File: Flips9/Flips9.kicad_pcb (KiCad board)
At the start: 2 copper layers, 100 x 100 mm, 45 parts, among them CN1 UFP2810, U1 74238, U11 74238, U12 74238, U13 TD62783, U14 ULN2803/2003, U21 74238, U22 74238, U23 TD62783, U24 ULN2803/2003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

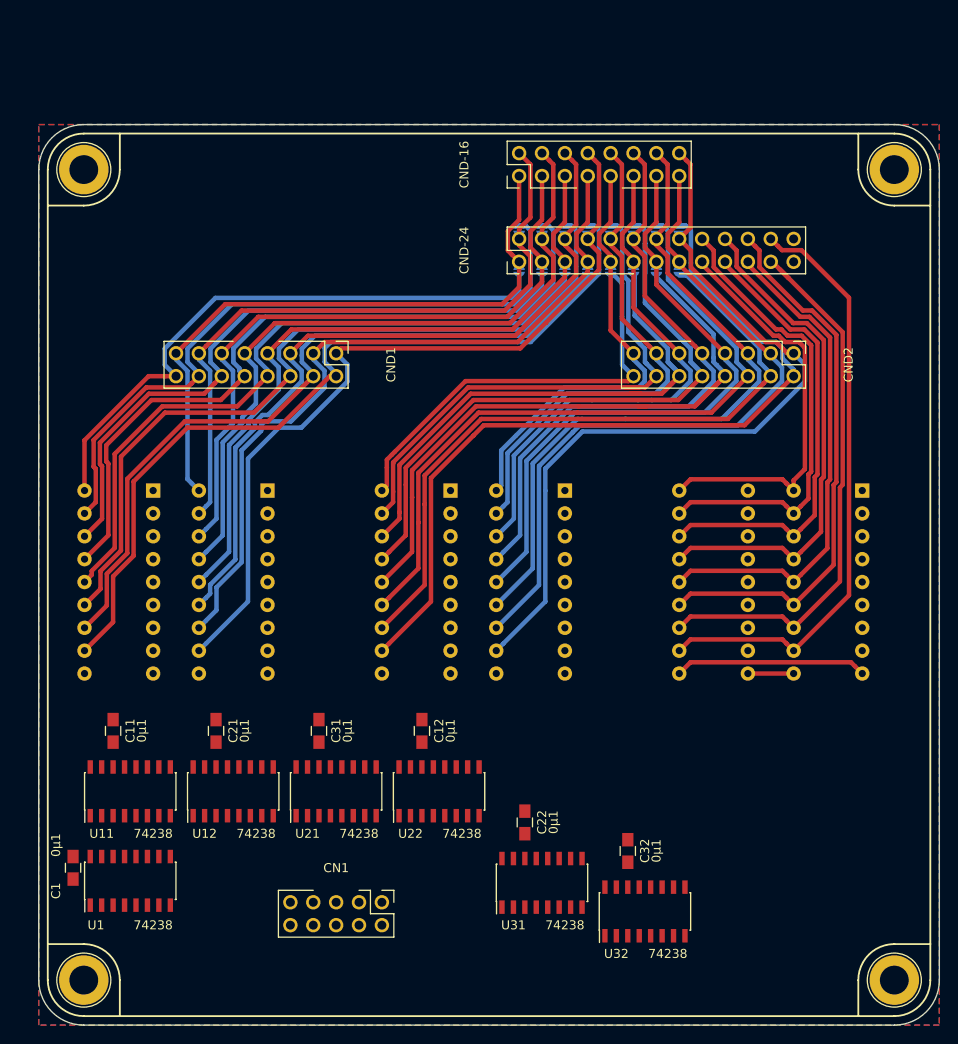
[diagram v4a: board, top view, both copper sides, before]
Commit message: routed more traces
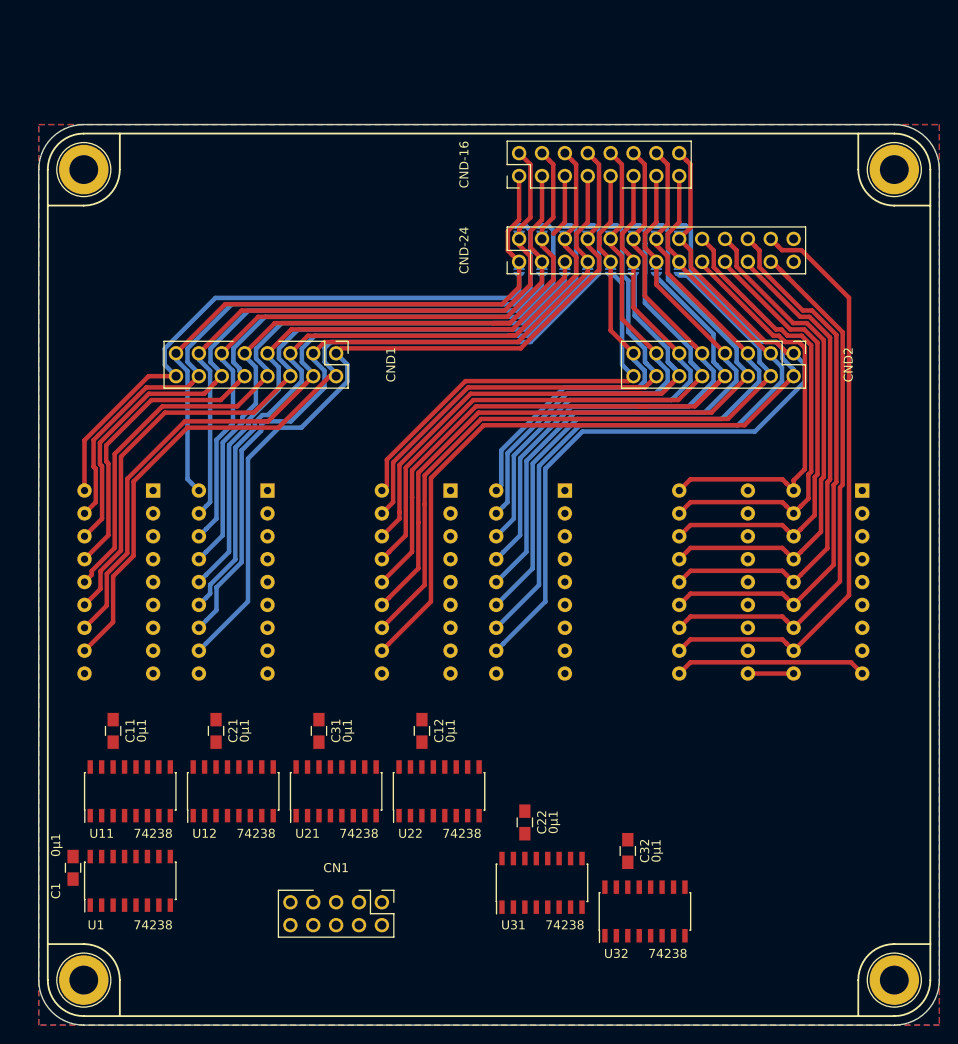
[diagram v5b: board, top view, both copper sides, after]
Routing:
- net /Y5: track 78.4 -> 75.0 mm
- net /Y4: track 79.3 -> 81.2 mm
- net /Y9: track 49.2 -> 50.0 mm
- net /Y6: track 84.0 -> 84.7 mm

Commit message: finish flips9 routing
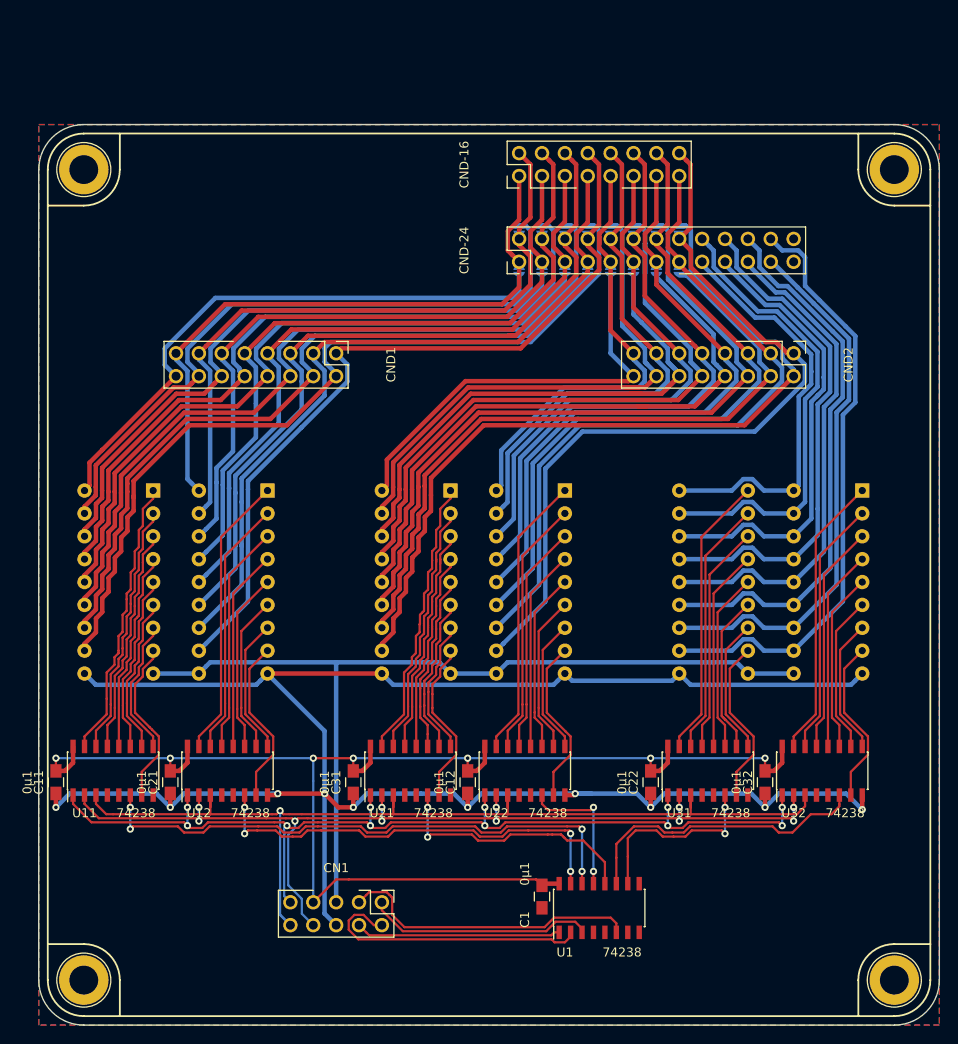
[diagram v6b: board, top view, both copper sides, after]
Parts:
- moved C1 52.2 mm to (106.7, 136.5)
- moved U1 52.2 mm to (113.0, 137.8)
- moved U32 25.1 mm to (137.8, 122.6)
- moved U31 22.2 mm to (125.1, 122.6)
- moved C32 17.0 mm to (131.4, 123.8), turned to 270 degrees
- moved C22 14.7 mm to (118.7, 123.8), turned to 270 degrees
- moved U22 9.80 mm to (104.8, 122.6)
- moved U21 8.57 mm to (92.1, 122.6)
- moved C11 8.53 mm to (52.7, 123.8), turned to 270 degrees
- moved C12 7.63 mm to (98.4, 123.8), turned to 270 degrees
- moved C21 7.63 mm to (65.4, 123.8), turned to 270 degrees
- moved C31 6.85 mm to (85.7, 123.8), turned to 270 degrees
- moved U11 2.98 mm to (59.1, 122.6)
- moved U12 2.37 mm to (71.8, 122.6)
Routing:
- net GND: track 21.4 -> 233.6 mm, vias 0 -> 10
- net VCC: track 0.00 -> 156.5 mm, vias 0 -> 7
- net /UnitY/A2: track 0.00 -> 110.8 mm, vias 0 -> 1
- net /UnitY/A0: track 0.00 -> 109.5 mm, vias 0 -> 11
- net /UnitY/A1: track 0.00 -> 109.3 mm, vias 0 -> 11
- net +24V: track 5.08 -> 100.1 mm
- net /UnitY/E0H: track 0.00 -> 62.5 mm, vias 0 -> 4
- net /UnitY/E0L: track 0.00 -> 48.1 mm, vias 0 -> 4
- net /UnitY/EN: track 0.00 -> 33.5 mm
- net /UnitY/E2L: track 0.00 -> 33.3 mm
- net Net-(U21-Pad15): track 0.00 -> 31.6 mm
- net Net-(U32-Pad15): track 0.00 -> 31.6 mm
- net Net-(U22-Pad15): track 0.00 -> 31.6 mm
- net Net-(U12-Pad15): track 0.00 -> 31.6 mm
- net Net-(U31-Pad15): track 0.00 -> 31.6 mm
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
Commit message: fixing GND THT pad orientation
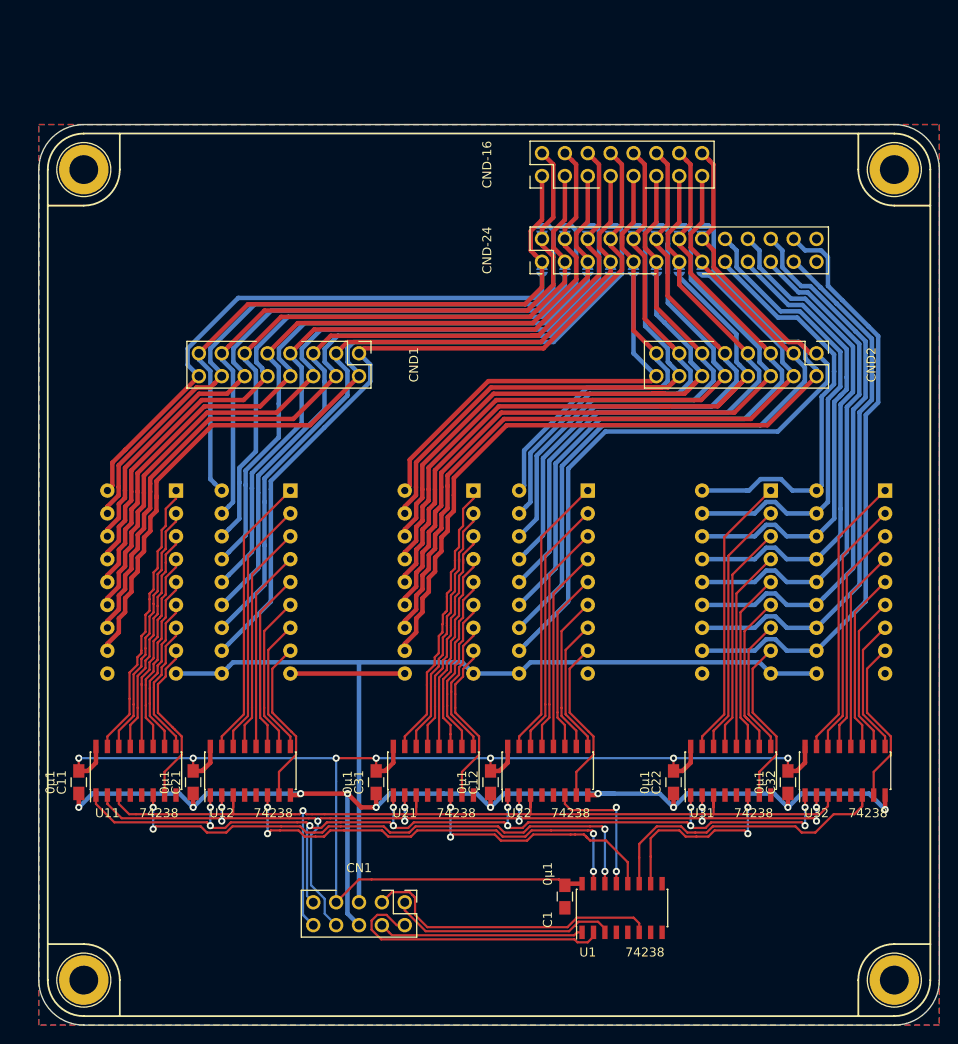
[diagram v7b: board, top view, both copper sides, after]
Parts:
- moved C32 2.54 mm to (134.0, 123.8)
- moved U32 2.54 mm to (140.3, 122.6)
- moved U33 2.54 mm to (132.1, 91.4)
- moved C12 2.54 mm to (101.0, 123.8)
- moved C31 2.54 mm to (88.3, 123.8)
- moved CND-16 2.54 mm to (106.7, 56.5)
- moved CND-24 2.54 mm to (106.7, 66.0)
- moved CND1 2.54 mm to (86.4, 76.2)
- moved JP101 2.54 mm to (106.7, 67.1)
- moved JP102 2.54 mm to (106.7, 62.5)
- moved JP105 2.54 mm to (111.8, 67.1)
- moved JP106 2.54 mm to (111.8, 62.5)
- moved JP109 2.54 mm to (116.8, 67.1)
- moved JP110 2.54 mm to (116.8, 62.5)
- moved JP113 2.54 mm to (121.9, 67.1)
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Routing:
- net GND: track 233.6 -> 140.2 mm

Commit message: compactify traces
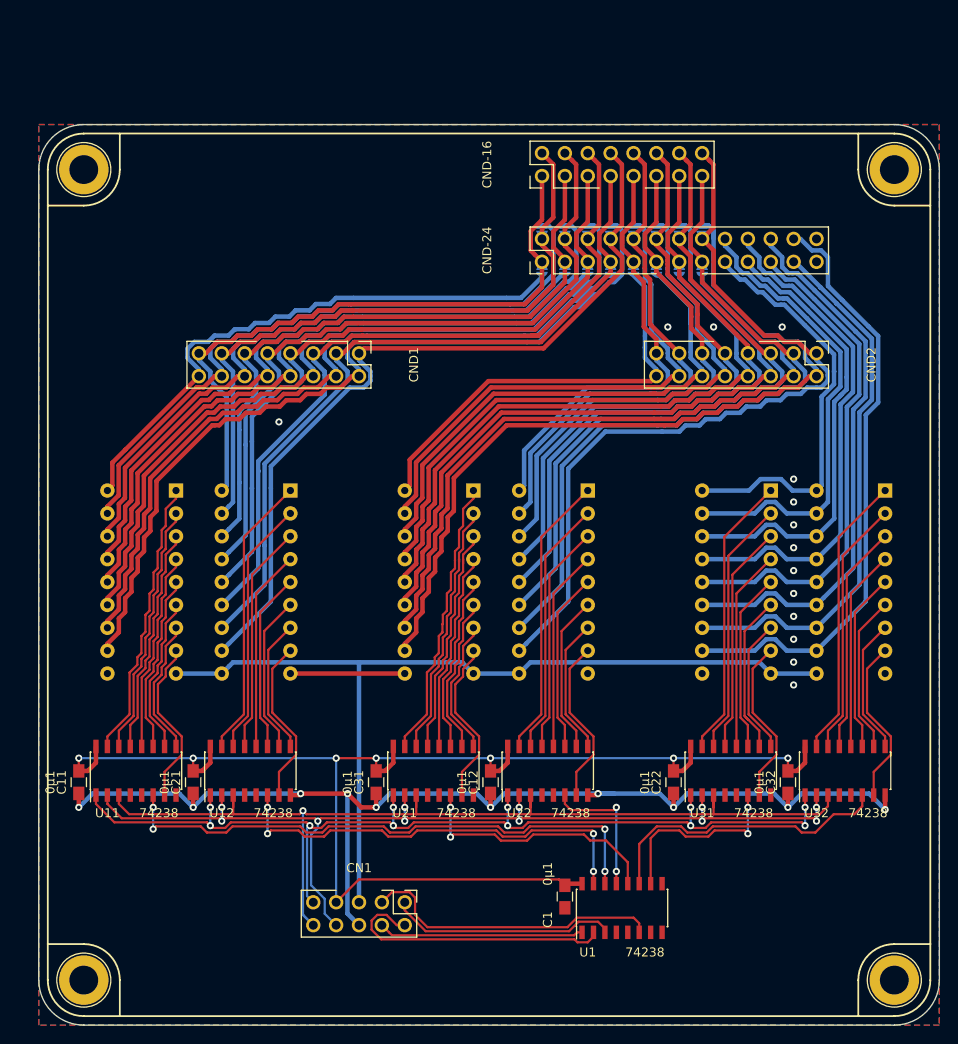
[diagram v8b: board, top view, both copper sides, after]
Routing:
- net /SX13: track 72.8 -> 67.5 mm
- net /SX12: track 74.1 -> 69.3 mm
- net /SX11: track 62.8 -> 59.2 mm
- net /SX10: track 61.6 -> 58.9 mm
- net /SX16: track 89.7 -> 91.9 mm
- net /Y15: track 79.5 -> 81.0 mm
- net /Y16: track 88.6 -> 89.7 mm
- net /Y14: track 77.4 -> 78.5 mm
- net /Y5: track 78.7 -> 79.7 mm
- net /Y8: track 87.9 -> 88.9 mm
- net /SX1: track 64.2 -> 63.3 mm
- net /SX15: track 77.8 -> 78.5 mm
- net /Y13: track 69.3 -> 70.0 mm
- net /Y7: track 82.7 -> 83.4 mm
- net /Y11: track 59.3 -> 60.0 mm
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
